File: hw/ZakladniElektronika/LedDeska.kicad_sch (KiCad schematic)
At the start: 13 parts, among them U1 LDC1614

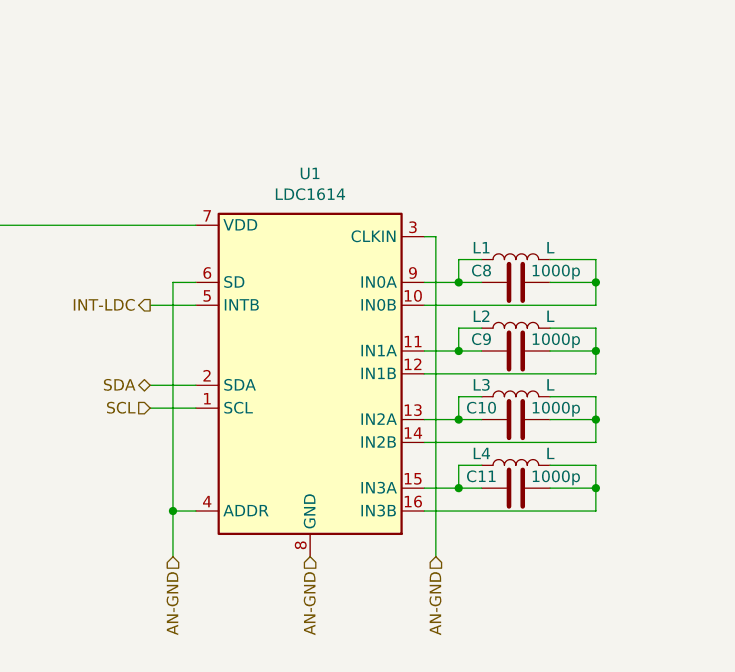
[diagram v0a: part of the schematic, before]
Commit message: Výmněna ochrany baterie
Předchozí ochranný čip JLCPCB nemělo na skladě
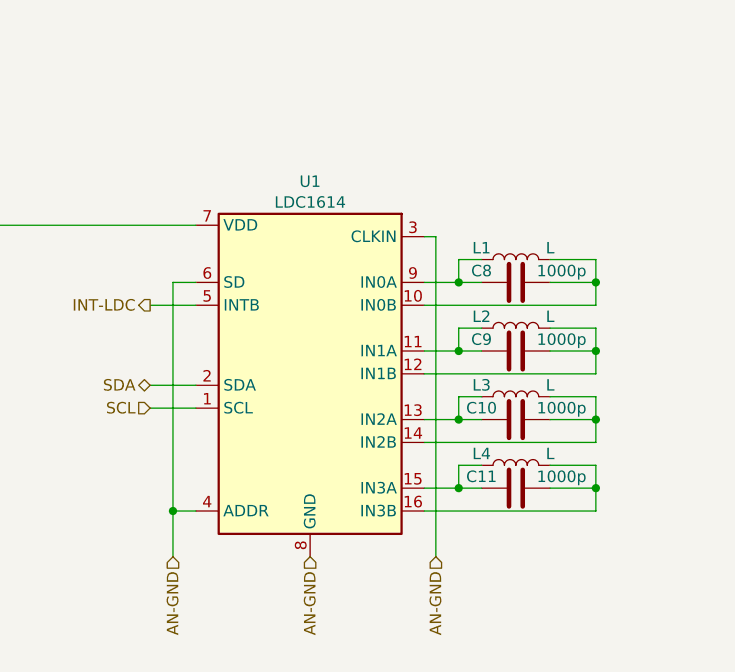
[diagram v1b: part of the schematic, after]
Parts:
- removed C10, C11, C8, C9: 1000p, Capacitor_SMD:C_0402_1005Metric, symbol B.B-rescue:C-Device-B.B-rescue
- added C10, C11, C8, C9: 1000p, Capacitor_SMD:C_0402_1005Metric, symbol Device:C
- L1, L2, L3, L4: symbol B.B-rescue:L-Device-B.B-rescue -> Device:L
- U1: symbol B.B-rescue:LDC1314-B.B-rescue -> RKL-SpecialThings:LDC1x14
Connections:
- net at L1.1, U1.10 (IN0B): now also C8.2
- net at L1.2, U1.9 (IN0A): now also C8.1
- net at L2.1, U1.12 (IN1B): now also C9.2
- net at L2.2, U1.11 (IN1A): now also C9.1
- net at L4.1, U1.16 (IN3B): now also C11.2
- net at L4.2, U1.15 (IN3A): now also C11.1
- net at L3.2, U1.13 (IN2A): now also C10.1
- net at L3.1, U1.14 (IN2B): now also C10.2

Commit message: PCB
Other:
- removed sheet LedRing-Radial
- added sheet LedRing-Axial1 (LedDeska/LedRing.kicad_sch)
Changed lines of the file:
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@@
     (stroke (width 0.1524) (type solid))
     (fill (color 0 0 0 0.0000))
-    (property "Sheetname" "LedRing-Radial" (at 165.1 47.5484 0)
+    (property "Sheetname" "LedRing-Axial1" (at 165.1 47.5484 0)
       (effects (font (size 1.27 1.27)) (justify left bottom))
     )
@@
       (effects (font (size 1.27 1.27)) (justify left))
     )
-    (pin "DOUT" output (at 198.12 55.88 0)
+    (pin "DOUT" output (at 198.12 57.15 0)
       (effects (font (size 1.27 1.27)) (justify right))
     )
@@
       )
       (project "ZakladniElektronika"
-        (path "/99cd3e15-4eb6-4cbb-8726-789aedd3df15/6a867e96-34ab-4d6c-a824-47bb4ec04e8c" (page "6"))
+        (path "/99cd3e15-4eb6-4cbb-8726-789aedd3df15/6a867e96-34ab-4d6c-a824-47bb4ec04e8c" (page "4"))
       )
     )

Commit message: Hodnoty senzorických cívek
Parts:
- L1, L2, L3, L4: value L -> 5.738 µH
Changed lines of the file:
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@@
   (junction (at 114.3 101.6) (diameter 0) (color 0 0 0 0)
   )
-  (no_connect (at 198.12 55.88))
+  (no_connect (at 198.12 57.15))
   (wire (pts (xy 171.45 115.57) (xy 175.26 115.57))
     (stroke (width 0) (type default))
@@
       (effects (font (size 1.27 1.27)))
     )
-    (property "Value" "L" (at 185.42 104.14 90)
+    (property "Value" "5.738 µH" (at 185.42 104.14 90)
       (effects (font (size 1.27 1.27)))
     )
@@
       (effects (font (size 1.27 1.27)))
     )
-    (property "Value" "L" (at 185.42 119.38 90)
+    (property "Value" "5.738 µH" (at 185.42 119.38 90)
       (effects (font (size 1.27 1.27)))
     )
@@
       (effects (font (size 1.27 1.27)))
     )
-    (property "Value" "L" (at 185.42 127 90)
+    (property "Value" "5.738 µH" (at 185.42 127 90)
       (effects (font (size 1.27 1.27)))
     )
@@
       (effects (font (size 1.27 1.27)))
     )
-    (property "Value" "L" (at 185.42 111.76 90)
-      (effects (font (size 1.27 1.27)))
-    )
+    (property "Value" "5.738 µH" (at 185.42 111.76 90)
+      (effects (font (size 1.27 1.27)))
+    )

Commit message: Hw PCB
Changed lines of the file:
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@@
 (kicad_sch
-	(version 20231120)
+	(version 20250114)
 	(generator "eeschema")
-	(generator_version "8.0")
+	(generator_version "9.0")
 	(paper "A4")
 	(junction
@@
 		(shape input)
 		(at 114.3 111.76 270)
-		(fields_autoplaced yes)
 		(effects
 			(font
@@
 		(shape input)
 		(at 158.75 138.43 270)
-		(fields_autoplaced yes)
 		(effects
 			(font
@@
 		(shape input)
 		(at 143.51 138.43 270)
-		(fields_autoplaced yes)
 		(effects
 			(font
@@
 		(shape input)
 		(at 81.28 66.04 270)
-		(fields_autoplaced yes)
 		(effects
 			(font
@@
 		(shape input)
 		(at 80.01 50.8 180)
-		(fields_autoplaced yes)
 		(effects
 			(font
@@
 		(shape input)
 		(at 88.9 101.6 180)
-		(fields_autoplaced yes)
 		(effects
 			(font
@@
 		(shape input)
 		(at 101.6 111.76 270)
-		(fields_autoplaced yes)
 		(effects
 			(font
@@
 		(shape input)
 		(at 118.11 57.15 180)
-		(fields_autoplaced yes)
 		(effects
 			(font
@@
 		(shape output)
 		(at 140.97 110.49 180)
-		(fields_autoplaced yes)
 		(effects
 			(font
@@
 		(shape input)
 		(at 162.56 66.04 270)
-		(fields_autoplaced yes)
 		(effects
 			(font
@@
 		(shape input)
 		(at 140.97 121.92 180)
-		(fields_autoplaced yes)
 		(effects
 			(font
@@
 		(shape input)
 		(at 172.72 138.43 270)
-		(fields_autoplaced yes)
 		(effects
 			(font
@@
 		(shape input)
 		(at 162.56 45.72 90)
-		(fields_autoplaced yes)
 		(effects
 			(font
@@
 		(shape bidirectional)
 		(at 140.97 119.38 180)
-		(fields_autoplaced yes)
 		(effects
 			(font
@@
 		(at 165.1 48.26)
 		(size 33.02 16.51)
+		(exclude_from_sim no)
+		(in_bom yes)
+		(on_board yes)
+		(dnp no)
 		(stroke
 			(width 0.1524)
@@
 		(at 120.65 48.26)
 		(size 33.02 16.51)
+		(exclude_from_sim no)
+		(in_bom yes)
+		(on_board yes)
+		(dnp no)
 		(stroke
 			(width 0.1524)
